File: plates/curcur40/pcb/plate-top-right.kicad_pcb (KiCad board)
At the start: 2 copper layers, 116.1 x 88.3 mm, 0 parts

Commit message: move trackball
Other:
- outline, holes or cut-outs redrawn
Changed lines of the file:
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@@
   (gr_line (start 82.862500 41.381250) (end 82.862500 62.562500) (stroke (width 0.2) (type solid)) (layer "Edge.Cuts"))
   (gr_arc (start 82.862500 62.562500) (mid 82.569607 63.269607) (end 81.862500 63.562500) (stroke (width 0.2) (type solid)) (layer "Edge.Cuts"))
-  (gr_line (start 81.862500 63.562500) (end 25.337500 63.562500) (stroke (width 0.2) (type solid)) (layer "Edge.Cuts"))
-  (gr_arc (start 25.337500 63.562500) (mid 24.630393 63.269607) (end 24.337500 62.562500) (stroke (width 0.2) (type solid)) (layer "Edge.Cuts"))
-  (gr_line (start 24.337500 62.562500) (end 24.337500 39.000000) (stroke (width 0.2) (type solid)) (layer "Edge.Cuts"))
-  (gr_arc (start 24.337500 39.000000) (mid 24.044607 38.292893) (end 23.337500 38.000000) (stroke (width 0.2) (type solid)) (layer "Edge.Cuts"))
-  (gr_line (start 23.337500 38.000000) (end 4.862500 38.000000) (stroke (width 0.2) (type solid)) (layer "Edge.Cuts"))
-  (gr_arc (start 4.862500 38.000000) (mid 4.155393 37.707107) (end 3.862500 37.000000) (stroke (width 0.2) (type solid)) (layer "Edge.Cuts"))
-  (gr_line (start 3.862500 37.000000) (end 3.862500 -16.568750) (stroke (width 0.2) (type solid)) (layer "Edge.Cuts"))
+  (gr_line (start 81.862500 63.562500) (end 23.837500 63.562500) (stroke (width 0.2) (type solid)) (layer "Edge.Cuts"))
+  (gr_arc (start 23.837500 63.562500) (mid 23.130393 63.269607) (end 22.837500 62.562500) (stroke (width 0.2) (type solid)) (layer "Edge.Cuts"))
+  (gr_line (start 22.837500 62.562500) (end 22.837500 38.400000) (stroke (width 0.2) (type solid)) (layer "Edge.Cuts"))
+  (gr_arc (start 22.837500 38.400000) (mid 22.544607 37.692893) (end 21.837500 37.400000) (stroke (width 0.2) (type solid)) (layer "Edge.Cuts"))
+  (gr_line (start 21.837500 37.400000) (end 4.862500 37.400000) (stroke (width 0.2) (type solid)) (layer "Edge.Cuts"))
+  (gr_arc (start 4.862500 37.400000) (mid 4.155393 37.107107) (end 3.862500 36.400000) (stroke (width 0.2) (type solid)) (layer "Edge.Cuts"))
+  (gr_line (start 3.862500 36.400000) (end 3.862500 -16.568750) (stroke (width 0.2) (type solid)) (layer "Edge.Cuts"))
   (gr_arc (start 102.537500 -13.643750) (mid 102.683947 -13.997303) (end 103.037500 -14.143750) (stroke (width 0.2) (type solid)) (layer "Edge.Cuts"))
   (gr_line (start 103.037500 -14.143750) (end 116.037500 -14.143750) (stroke (width 0.2) (type solid)) (layer "Edge.Cuts"))

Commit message: fix all
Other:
- outline, holes or cut-outs redrawn

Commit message: fix all
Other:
- board size 116.1 x 88.3 mm -> 125.1 x 92.6 mm
- rule pad_to_mask_clearance: 0.2 -> 0

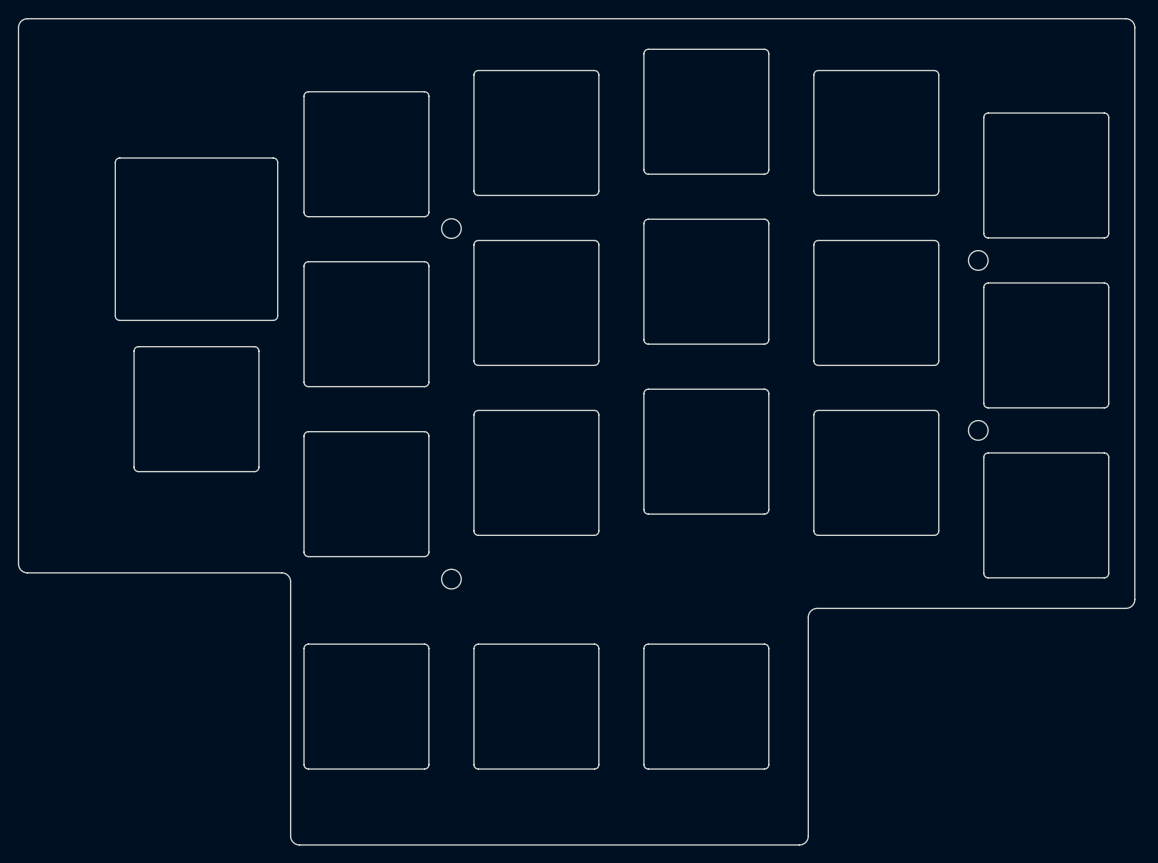
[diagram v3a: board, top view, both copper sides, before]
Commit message: Restore TRRS cutouts and relocate mounting holes to perimeter
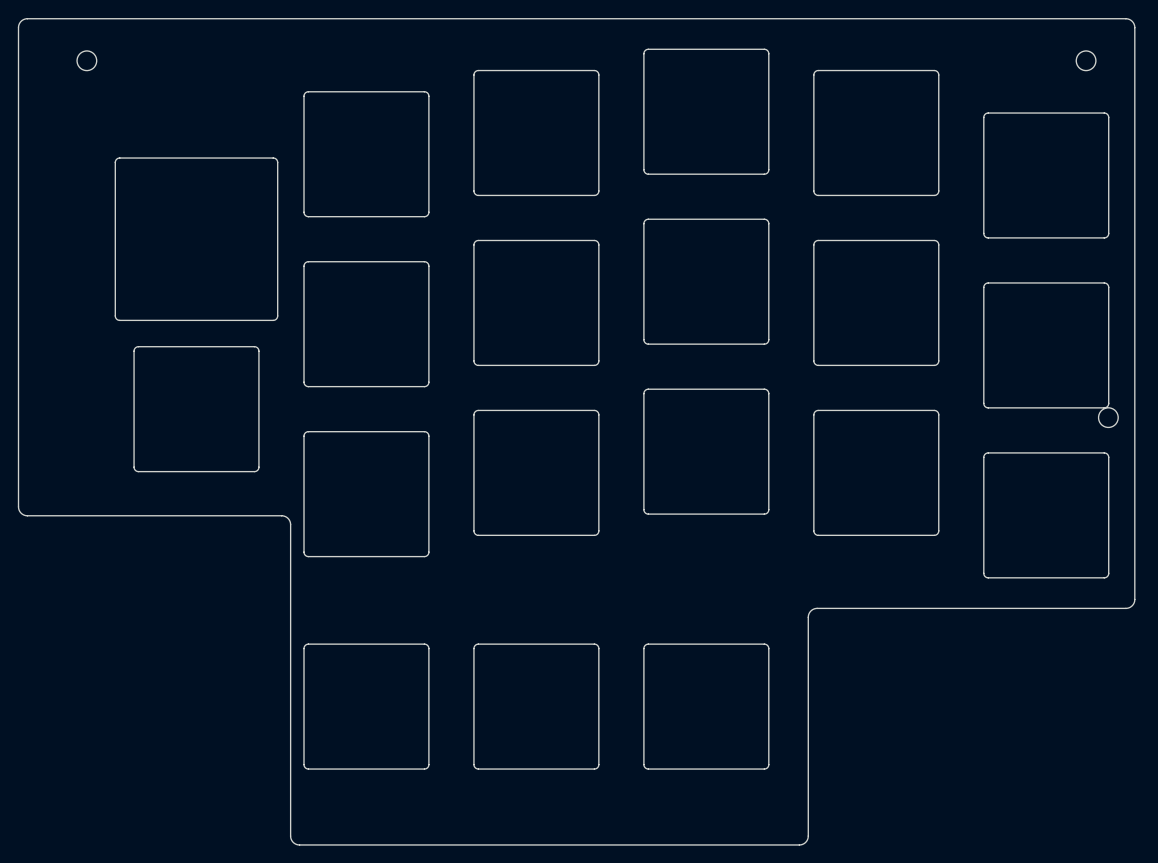
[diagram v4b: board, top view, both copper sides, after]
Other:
- outline, holes or cut-outs redrawn
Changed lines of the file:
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@@
 	)
 	(gr_line
-		(start -5.6625 36.4)
+		(start -5.6625 30)
 		(end -5.6625 -23.7125)
 		(stroke
@@
 	)
 	(gr_arc
-		(start -4.6625 37.4)
-		(mid -5.369607 37.107107)
-		(end -5.6625 36.4)
-		(stroke
-			(width 0.15)
-			(type default)
-		)
+		(start -4.6625 31)
+		(mid -5.369607 30.707107)
+		(end -5.6625 30)
+		(stroke
+			(width 0.15)
+			(type default)
+		)
+		(layer "Edge.Cuts")
+	)
+	(gr_circle
+		(center 2 -20)
+		(end 3.1 -20)
+		(stroke
+			(width 0.15)
+			(type default)
+		)
+		(fill no)
 		(layer "Edge.Cuts")
 	)
@@
 	)
 	(gr_line
-		(start 23.8375 37.4)
-		(end -4.6625 37.4)
-		(stroke
-			(width 0.15)
-			(type default)
-		)
-		(layer "Edge.Cuts")
-	)
-	(gr_arc
-		(start 23.8375 37.4)
-		(mid 24.544607 37.692893)
-		(end 24.8375 38.4)
+		(start 23.8375 31)
+		(end -4.6625 31)
+		(stroke
+			(width 0.15)
+			(type default)
+		)
+		(layer "Edge.Cuts")
+	)
+	(gr_arc
+		(start 23.8375 31)
+		(mid 24.544607 31.292893)
+		(end 24.8375 32)
 		(stroke
 			(width 0.15)
@@
 	(gr_line
 		(start 24.8375 66.9)
-		(end 24.8375 38.4)
+		(end 24.8375 32)
 		(stroke
 			(width 0.15)
@@
 		(layer "Edge.Cuts")
 	)
-	(gr_circle
-		(center 42.8625 -1.190625)
-		(end 43.9625 -1.190625)
-		(stroke
-			(width 0.15)
-			(type default)
-		)
-		(fill no)
-		(layer "Edge.Cuts")
-	)
-	(gr_circle
-		(center 42.8625 38.1)
-		(end 43.9625 38.1)
-		(stroke
-			(width 0.15)
-			(type default)
-		)
-		(fill no)
-		(layer "Edge.Cuts")
-	)
 	(gr_arc
 		(start 45.3875 -18.40625)
@@
 		(layer "Edge.Cuts")
 	)
-	(gr_circle
-		(center 101.9175 2.38125)
-		(end 103.0175 2.38125)
-		(stroke
-			(width 0.15)
-			(type default)
-		)
-		(fill no)
-		(layer "Edge.Cuts")
-	)
-	(gr_circle
-		(center 101.9175 21.43125)
-		(end 103.0175 21.43125)
-		(stroke
-			(width 0.15)
-			(type default)
-		)
-		(fill no)
-		(layer "Edge.Cuts")
-	)
 	(gr_arc
 		(start 102.5375 -13.64375)
@@
 		(layer "Edge.Cuts")
 	)
+	(gr_circle
+		(center 114 -20)
+		(end 115.1 -20)
+		(stroke
+			(width 0.15)
+			(type default)
+		)
+		(fill no)
+		(layer "Edge.Cuts")
+	)
 	(gr_arc
 		(start 116.0375 -14.14375)
@@
 		(layer "Edge.Cuts")
 	)
+	(gr_circle
+		(center 116.5 20)
+		(end 117.6 20)
+		(stroke
+			(width 0.15)
+			(type default)
+		)
+		(fill no)
+		(layer "Edge.Cuts")
+	)

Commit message: fix trrs top plate
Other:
- outline, holes or cut-outs redrawn
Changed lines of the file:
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@@
 	)
 	(gr_line
-		(start -5.6625 30)
+		(start -5.6625 36.4)
 		(end -5.6625 -23.7125)
 		(stroke
@@
 	)
 	(gr_arc
-		(start -4.6625 31)
-		(mid -5.369607 30.707107)
-		(end -5.6625 30)
-		(stroke
-			(width 0.15)
-			(type default)
-		)
-		(layer "Edge.Cuts")
-	)
-	(gr_circle
-		(center 2 -20)
-		(end 3.1 -20)
-		(stroke
-			(width 0.15)
-			(type default)
-		)
-		(fill no)
+		(start -4.6625 37.4)
+		(mid -5.369607 37.107107)
+		(end -5.6625 36.4)
+		(stroke
+			(width 0.15)
+			(type default)
+		)
 		(layer "Edge.Cuts")
 	)
@@
 		(layer "Edge.Cuts")
 	)
-	(gr_line
-		(start 23.8375 31)
-		(end -4.6625 31)
-		(stroke
-			(width 0.15)
-			(type default)
-		)
-		(layer "Edge.Cuts")
-	)
-	(gr_arc
-		(start 23.8375 31)
-		(mid 24.544607 31.292893)
-		(end 24.8375 32)
+	(gr_circle
+		(center 23.8125 -22.5)
+		(end 24.9125 -22.5)
+		(stroke
+			(width 0.15)
+			(type default)
+		)
+		(fill no)
+		(layer "Edge.Cuts")
+	)
+	(gr_line
+		(start 23.8375 37.4)
+		(end -4.6625 37.4)
+		(stroke
+			(width 0.15)
+			(type default)
+		)
+		(layer "Edge.Cuts")
+	)
+	(gr_arc
+		(start 23.8375 37.4)
+		(mid 24.544607 37.692893)
+		(end 24.8375 38.4)
 		(stroke
 			(width 0.15)
@@
 	(gr_line
 		(start 24.8375 66.9)
-		(end 24.8375 32)
+		(end 24.8375 38.4)
 		(stroke
 			(width 0.15)
@@
 		(layer "Edge.Cuts")
 	)
+	(gr_circle
+		(center 98 38)
+		(end 99.1 38)
+		(stroke
+			(width 0.15)
+			(type default)
+		)
+		(fill no)
+		(layer "Edge.Cuts")
+	)
+	(gr_circle
+		(center 100 -22.5)
+		(end 101.1 -22.5)
+		(stroke
+			(width 0.15)
+			(type default)
+		)
+		(fill no)
+		(layer "Edge.Cuts")
+	)
 	(gr_arc
 		(start 102.5375 -13.64375)
@@
 		(layer "Edge.Cuts")
 	)
-	(gr_circle
-		(center 114 -20)
-		(end 115.1 -20)
-		(stroke
-			(width 0.15)
-			(type default)
-		)
-		(fill no)
-		(layer "Edge.Cuts")
-	)
 	(gr_arc
 		(start 116.0375 -14.14375)
@@
 		(layer "Edge.Cuts")
 	)
-	(gr_circle
-		(center 116.5 20)
-		(end 117.6 20)
-		(stroke
-			(width 0.15)
-			(type default)
-		)
-		(fill no)
-		(layer "Edge.Cuts")
-	)
